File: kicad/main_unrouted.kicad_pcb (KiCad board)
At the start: 2 copper layers, 119.4 x 99.1 mm, 41 parts, among them J1 Barrel_Jack, SW1 Reset, SW6 SW_DIP_x08, U1 KM1810VM88, U10 L7805, U11 15 MHz, U12 8255, U13 74HC273, U14 74HC244, U2 W27C512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

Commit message: Corrected version of v1 PCB
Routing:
- net GND: track 528.8 -> 137.4 mm
- net +5V: track 482.1 -> 115.9 mm
- net AD_{7}: track 231.3 -> 0.00 mm
- net AD_{4}: track 208.0 -> 0.00 mm, vias 2 -> 0
- net AD_{5}: track 196.6 -> 0.00 mm
- net AD_{6}: track 196.3 -> 0.00 mm
- net AD_{3}: track 194.8 -> 0.00 mm, vias 1 -> 0
- net AD_{2}: track 176.7 -> 0.00 mm, vias 2 -> 0
- net ~{RD}: track 175.7 -> 0.00 mm, vias 1 -> 0
- net A_{15}: track 171.3 -> 0.00 mm
- net AD_{0}: track 167.7 -> 0.00 mm, vias 2 -> 0
- net AD_{1}: track 166.1 -> 0.00 mm, vias 2 -> 0
- net A_{0}: track 158.5 -> 0.00 mm, vias 3 -> 0
- net A_{1}: track 152.0 -> 0.00 mm, vias 2 -> 0
- net A_{17}: track 148.6 -> 0.00 mm, vias 2 -> 0
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
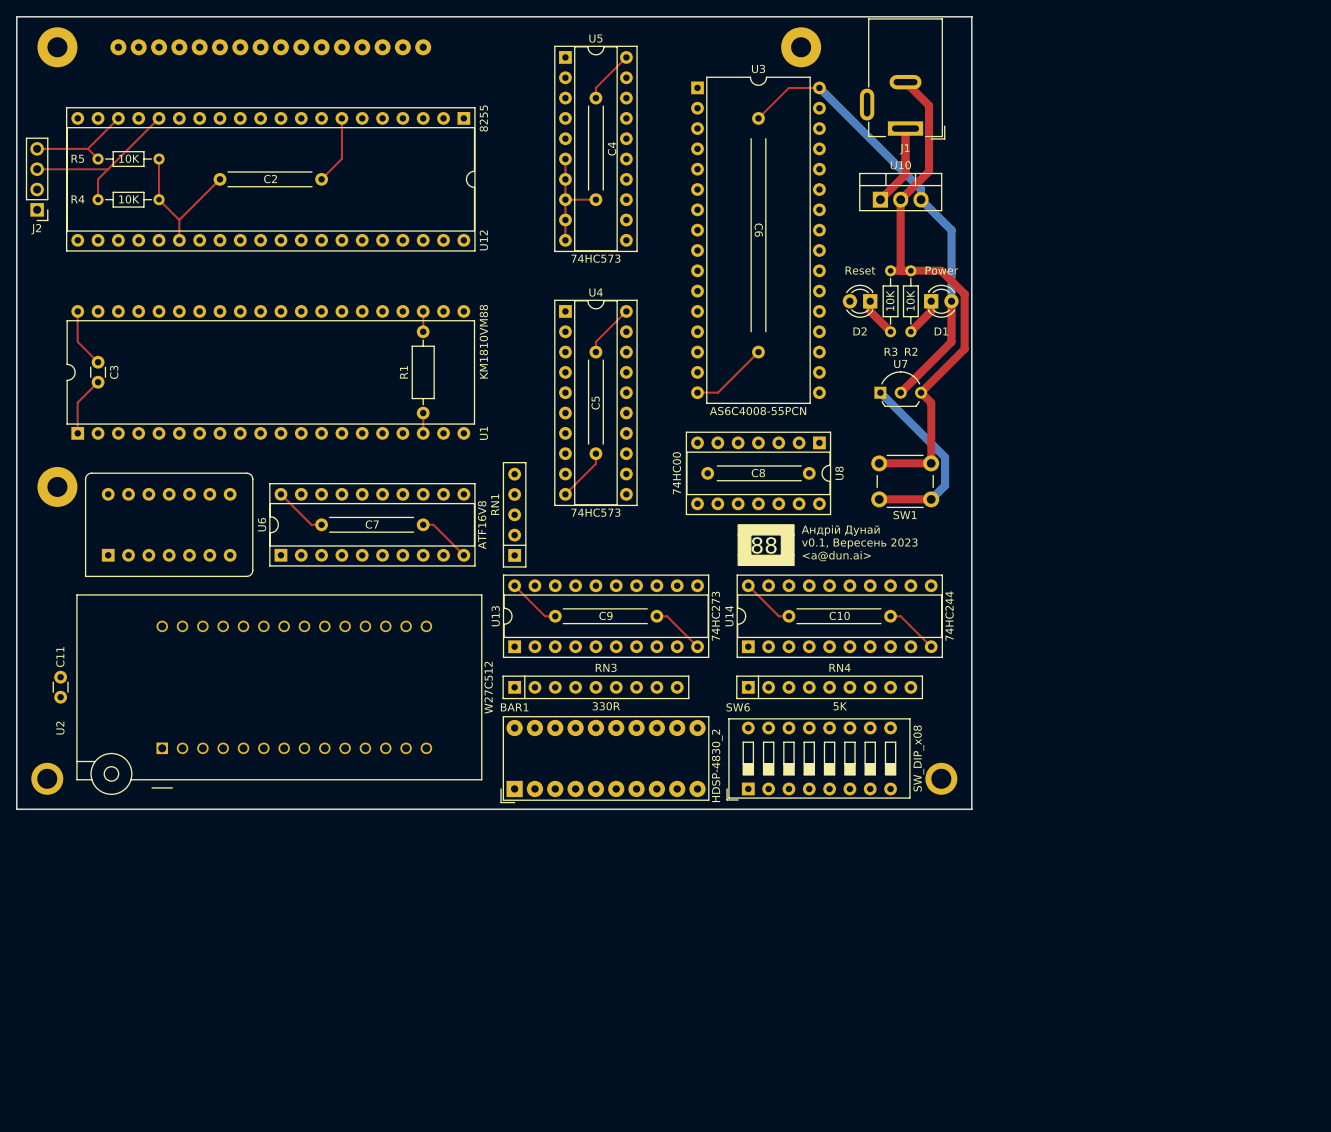
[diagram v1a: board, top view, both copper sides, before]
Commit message: Add I/O sheet
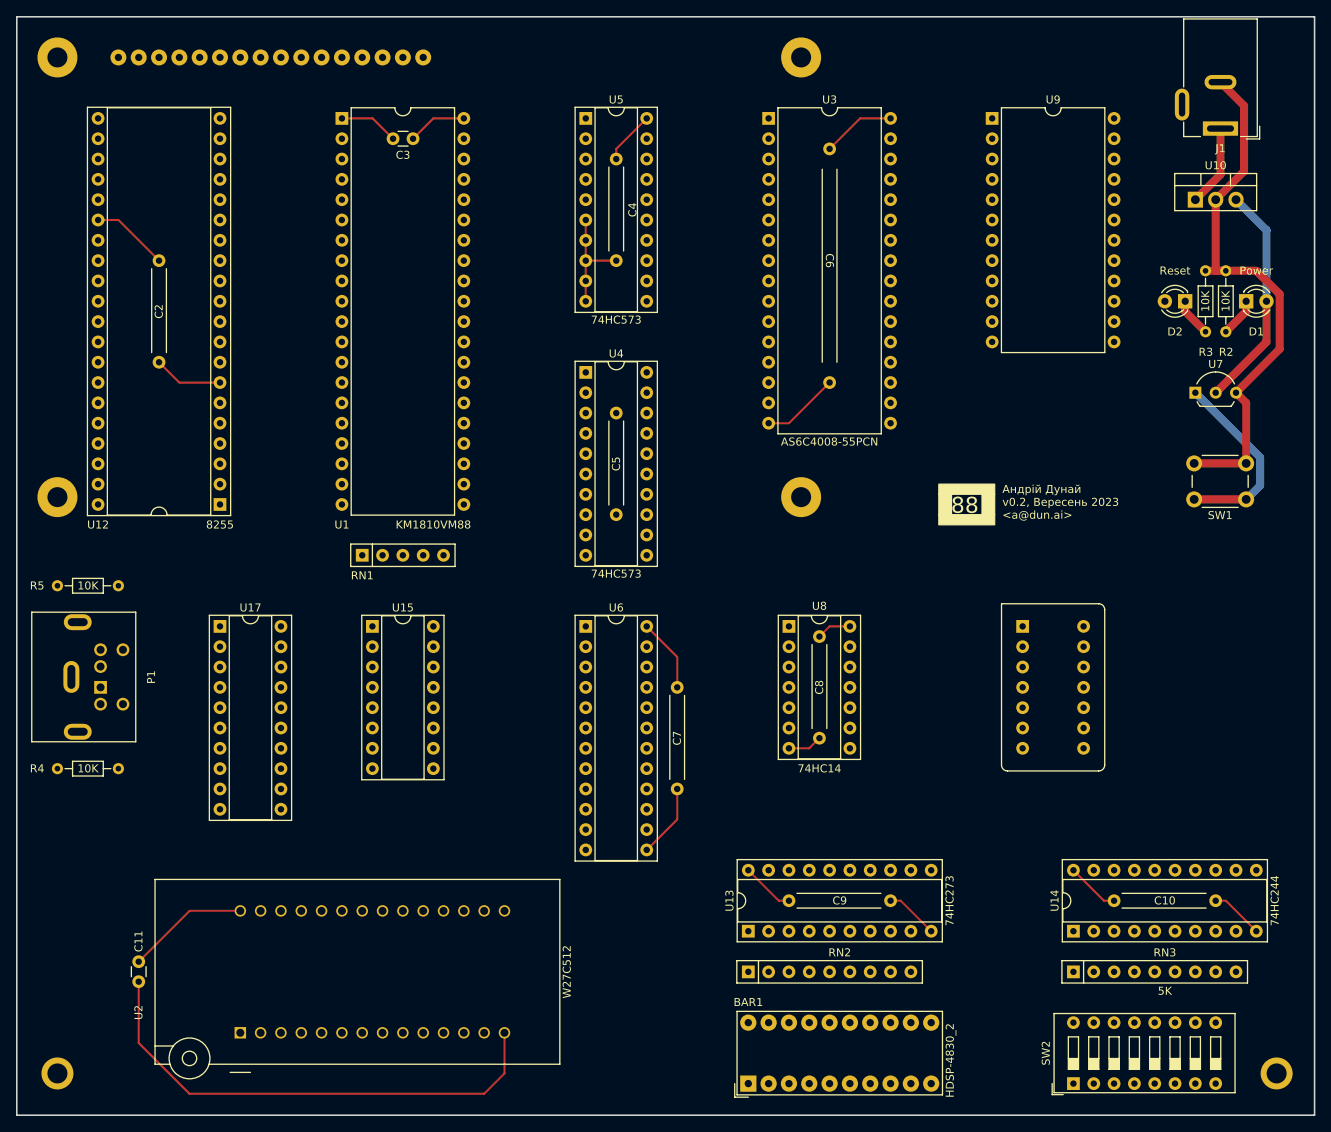
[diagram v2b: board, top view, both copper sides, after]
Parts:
- removed J2: ~, Connector_PinHeader_2.54mm:PinHeader_1x04_P2.54mm_Vertical
- removed R1: 10K, Resistor_THT:R_Axial_DIN0207_L6.3mm_D2.5mm_P10.16mm_Horizontal
- removed RN4: 5K, Resistor_THT:R_Array_SIP9
- removed SW6: SW_DIP_x08, Button_Switch_THT:SW_DIP_SPSTx08_Slide_9.78x22.5mm_W7.62mm_P2.54mm
- added P1: Mini-DIN_6pins_ver3, Custom_Footprints:Connector_Mini-DIN_Female_6Pin_2rows, F.Cu at (25.7, -25.4)
- added RN2: 330R, Resistor_THT:R_Array_SIP9, F.Cu at (106.7, 10.2)
- added SW2: SW_DIP_x08, Button_Switch_THT:SW_DIP_SPSTx08_Slide_9.78x22.5mm_W7.62mm_P2.54mm, F.Cu at (147.3, 24.1)
- added U15: 74HC148, Package_DIP:DIP-16_W7.62mm_Socket, F.Cu at (59.7, -33.0)
- added U17: 74HC244, Package_DIP:DIP-20_W7.62mm_Socket, F.Cu at (40.6, -33.0)
- added U9: 8253, Package_DIP:DIP-24_W15.24mm, F.Cu at (137.2, -96.5)
- RN3: value 330R -> 5K
- U6: value ATF16V8 -> GAL22V10; footprint Package_DIP:DIP-20_W7.62mm_Socket -> Package_DIP:DIP-24_W7.62mm_Socket
- U8: value 74HC00 -> 74HC14
- moved U11 112.1 mm to (144.6, -25.4), turned to -90 degrees
- moved RN3 78.4 mm to (147.3, 10.2)
- moved R4 71.3 mm to (27.9, -15.2)
- moved U12 57.1 mm to (40.6, -48.3), turned to 180 degrees
- moved H2 55.8 mm to (172.7, 22.9)
- moved C10 54.0 mm to (152.4, 1.27)
- moved U14 54.0 mm to (147.3, 5.08)
- moved R5 53.6 mm to (27.9, -38.1)
- moved U1 51.4 mm to (55.9, -96.5), turned to 0 degrees
- moved C7 48.9 mm to (97.8, -25.4), turned to -90 degrees
- moved C3 48.3 mm to (64.8, -94.0), turned to 180 degrees
- moved BAR1 47.0 mm to (106.7, 24.1)
- moved C9 46.0 mm to (111.8, 1.27)
- moved U13 46.0 mm to (106.7, 5.08)
- moved R3 39.4 mm to (163.8, -69.8)
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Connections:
- BAR1 pad 13: Net-(RN3-R8) -> Net-(RN2-R8)
- BAR1 pad 14: Net-(RN3-R7) -> Net-(RN2-R7)
- BAR1 pad 15: Net-(RN3-R6) -> Net-(RN2-R6)
- BAR1 pad 16: Net-(RN3-R5) -> Net-(RN2-R5)
- BAR1 pad 17: Net-(RN3-R4) -> Net-(RN2-R4)
- BAR1 pad 18: Net-(RN3-R3) -> Net-(RN2-R3)
- BAR1 pad 19: Net-(RN3-R2) -> Net-(RN2-R2)
- BAR1 pad 20: Net-(RN3-R1) -> Net-(RN2-R1)
- SW1 pad 1: Net-(U7-~{RST}) -> ~{RES}
- U1 pad 18: INT -> INTR
- U1 pad 24: unconnected-(U1-~{INTA}-Pad24) -> ~{INTA}
- U12 pad 14: INT -> Net-(U12-PC0)
- U13 pad 1: Net-(U13-~{Mr}) -> ~{RES}
- U14 pad 11: Net-(RN4-R8) -> Net-(RN3-R8)
- U14 pad 13: Net-(RN4-R7) -> Net-(RN3-R7)
- U14 pad 15: Net-(RN4-R6) -> Net-(RN3-R6)
- U14 pad 17: Net-(RN4-R5) -> Net-(RN3-R5)
- U14 pad 2: Net-(RN4-R1) -> Net-(RN3-R1)
- U14 pad 4: Net-(RN4-R2) -> Net-(RN3-R2)
- U14 pad 6: Net-(RN4-R3) -> Net-(RN3-R3)
- U14 pad 8: Net-(RN4-R4) -> Net-(RN3-R4)
- U6 pad 10: GND -> unconnected-(U6-I-Pad10)
- U6 pad 11: GND -> unconnected-(U6-I-Pad11)
- U6 pad 12: unconnected-(U6-IO8-Pad12) -> GND
- U6 pad 13: Net-(U6-IO7) -> GND
- U6 pad 15: IO~{EN} -> Net-(U6-I/O/Q-Pad15)
- U6 pad 16: IN~{EN} -> unconnected-(U6-I/O/Q-Pad16)
- U6 pad 17: OUT~{EN} -> Net-(U6-I/O/Q-Pad17)
- U6 pad 18: RAM~{EN} -> TIMER~{EN}
- U6 pad 19: ROM~{EN} -> IO~{EN}
- U6 pad 20: +5V -> IN~{EN}
- U7 pad 1: Net-(U7-~{RST}) -> ~{RES}
- U8 pad 1: Net-(U6-IO7) -> Net-(U6-I/O/Q-Pad15)
- U8 pad 10: Net-(U7-~{RST}) -> ~{INT1}
- U8 pad 11: unconnected-(U8-Pad11) -> Net-(U12-PC0)
- U8 pad 13: unconnected-(U8-Pad13) -> GND
- U8 pad 2: Net-(U6-IO7) -> CLK
- U8 pad 3: CLK -> Net-(U6-I/O/Q-Pad17)
- U8 pad 4: RES -> TIMERCLK
- U8 pad 5: RES -> ~{RES}
- U8 pad 6: Net-(U13-~{Mr}) -> RES
- U8 pad 8: RES -> ~{INT0}
- U8 pad 9: Net-(U7-~{RST}) -> Net-(U9-OUT0)
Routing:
- net GND: track 137.4 -> 197.3 mm
- net ~{RES}: track 0.00 -> 23.9 mm
- net Net-(U7-~{RST}): track 23.9 -> 0.00 mm
- net PS2CLK: track 22.2 -> 0.00 mm
- net PS2DATA: track 13.5 -> 0.00 mm
- net +5V: track 115.9 -> 103.5 mm
- net INT: track 2.54 -> 0.00 mm
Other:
- board size 119.4 x 99.1 mm -> 162.2 x 137.3 mm
- board text added: "Андрій Дунай v0.2, Вересень 2023 <a@dun.ai>"
- board text removed: "Андрій Дунай v0.1, Вересень 2023 <a@dun.ai>"

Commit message: Add UART & uSD card
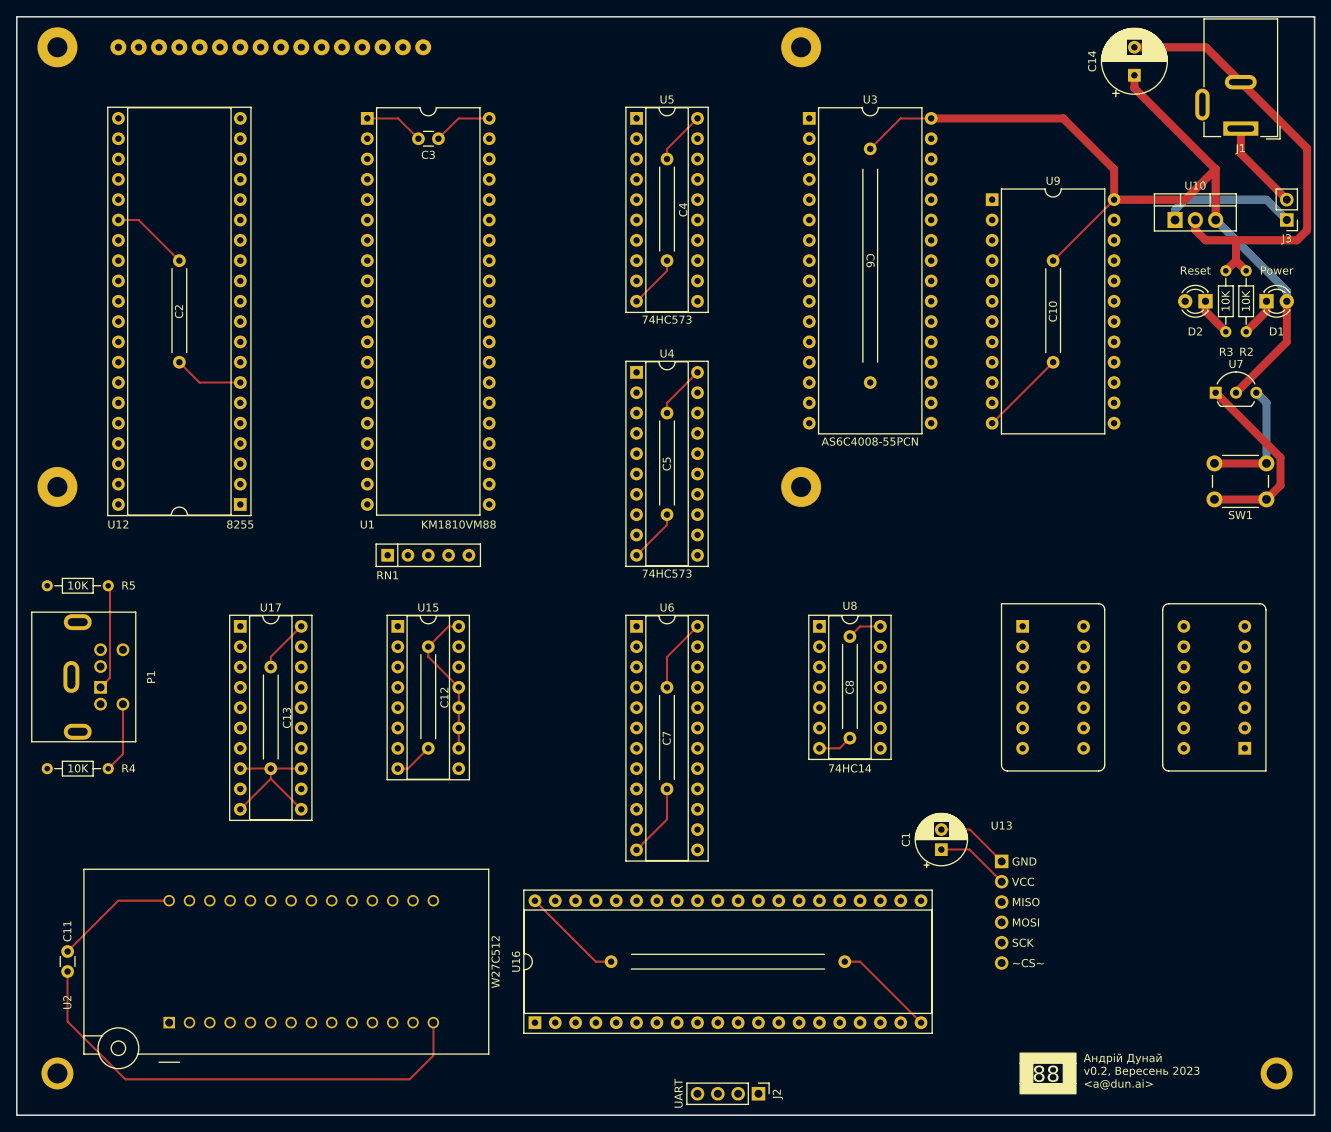
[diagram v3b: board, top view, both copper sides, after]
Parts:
- removed BAR1: HDSP-4830_2, Display:HDSP-4830
- removed RN2: 330R, Resistor_THT:R_Array_SIP9
- removed RN3: 5K, Resistor_THT:R_Array_SIP9
- removed SW2: SW_DIP_x08, Button_Switch_THT:SW_DIP_SPSTx08_Slide_9.78x22.5mm_W7.62mm_P2.54mm
- removed U14: 74HC244, Package_DIP:DIP-20_W7.62mm_Socket
- added C1: 10 uF, Capacitor_THT:CP_Radial_D6.3mm_P2.50mm, F.Cu at (130.8, -5.12)
- added C12: 0.1 uF, footprints:C_Disc_Long, F.Cu at (66.7, -30.5)
- added C13: 0.1 uF, footprints:C_Disc_Long, F.Cu at (47.0, -27.9)
- added C14: 10 uF, Capacitor_THT:CP_Radial_D8.0mm_P3.50mm, F.Cu at (154.9, -101.9)
- added J2: UART, Connector_PinHeader_2.54mm:PinHeader_1x04_P2.54mm_Vertical, F.Cu at (108.0, 25.4)
- added J3: ~, Connector_PinHeader_2.54mm:PinHeader_1x02_P2.54mm_Vertical, F.Cu at (174.0, -83.8)
- added U16: 16550, Package_DIP:DIP-40_W15.24mm_Socket, F.Cu at (80.0, 16.5)
- added U18: 1.8432 MHz, footprints:Oscillator_DIP-8-14, F.Cu at (165.1, -25.4)
- C9: footprint footprints:C_Disc_Long -> footprints:C_Disc_VeryLong
- U13: value 74HC273 -> uSD adapter; footprint Package_DIP:DIP-20_W7.62mm_Socket -> footprints:MicroSD-Adapter
- moved C10 80.4 mm to (144.8, -78.7), turned to -90 degrees
- moved U13 32.5 mm to (135.8, -9.36), turned to 0 degrees
- moved C9 17.6 mm to (95.9, 8.89)
- moved U9 10.2 mm to (137.2, -86.4)
- moved C11 8.98 mm to (21.6, 7.62)
- moved U2 8.98 mm to (34.3, 16.5)
- moved R4 8.89 mm to (19.1, -15.2), turned to 0 degrees
- moved R5 8.89 mm to (19.1, -38.1), turned to 0 degrees
- moved C4 6.35 mm to (96.5, -91.4)
- moved C5 6.35 mm to (96.5, -59.7)
- moved U4 6.35 mm to (92.7, -64.8)
- moved U5 6.35 mm to (92.7, -96.5)
- moved U6 6.35 mm to (92.7, -33.0)
- moved C6 5.08 mm to (121.9, -86.4)
- moved U3 5.08 mm to (114.3, -96.5)
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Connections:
- net Net-(U11-OUT) renamed MCLK
- J1 pad 1: Net-(U10-IN) -> Net-(J3-Pin_2)
- U1 pad 31: unconnected-(U1-HOLD-Pad31) -> GND
- U10 pad 1: Net-(U10-IN) -> Net-(J3-Pin_1)
- U13 pad 1: ~{RES} -> GND
- U13 pad 2: Net-(U13-Q0) -> +5V
- U13 pad 3: AD_{0} -> Net-(U13-MISO)
- U13 pad 4: AD_{1} -> Net-(U13-MOSI)
- U15 pad 2: +5V -> ~{INT2}
- U6 pad 10: unconnected-(U6-I-Pad10) -> IO/~{M}
- U6 pad 16: unconnected-(U6-I/O/Q-Pad16) -> Net-(U6-I/O/Q-Pad16)
- U6 pad 17: Net-(U6-I/O/Q-Pad17) -> unconnected-(U6-I/O/Q-Pad17)
- U6 pad 18: TIMER~{EN} -> unconnected-(U6-I/O/Q-Pad18)
- U6 pad 19: IO~{EN} -> UART~{EN}
- U6 pad 20: IN~{EN} -> TIMER~{EN}
- U6 pad 21: OUT~{EN} -> IO~{EN}
- U6 pad 3: A_{16} -> A_{9}
- U6 pad 4: A_{17} -> A_{16}
- U6 pad 5: A_{18} -> A_{17}
- U6 pad 6: A_{19} -> A_{18}
- U6 pad 7: ~{RD} -> A_{19}
- U6 pad 8: ~{WR} -> ~{RD}
- U6 pad 9: IO/~{M} -> ~{WR}
- U8 pad 12: unconnected-(U8-Pad12) -> ~{INT2}
- U8 pad 13: GND -> Net-(U16-INTR)
- U8 pad 3: Net-(U6-I/O/Q-Pad17) -> Net-(U6-I/O/Q-Pad16)
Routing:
- net +5V: track 103.5 -> 220.7 mm
- net GND: track 197.3 -> 235.8 mm
- net Net-(J3-Pin_1): track 0.00 -> 16.8 mm
- net PS2DATA: track 0.00 -> 13.3 mm
- net Net-(J3-Pin_2): track 0.00 -> 11.3 mm
- net Net-(U10-IN): track 10.2 -> 0.00 mm
- net PS2CLK: track 0.00 -> 8.82 mm

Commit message: Move chips to center/bottom
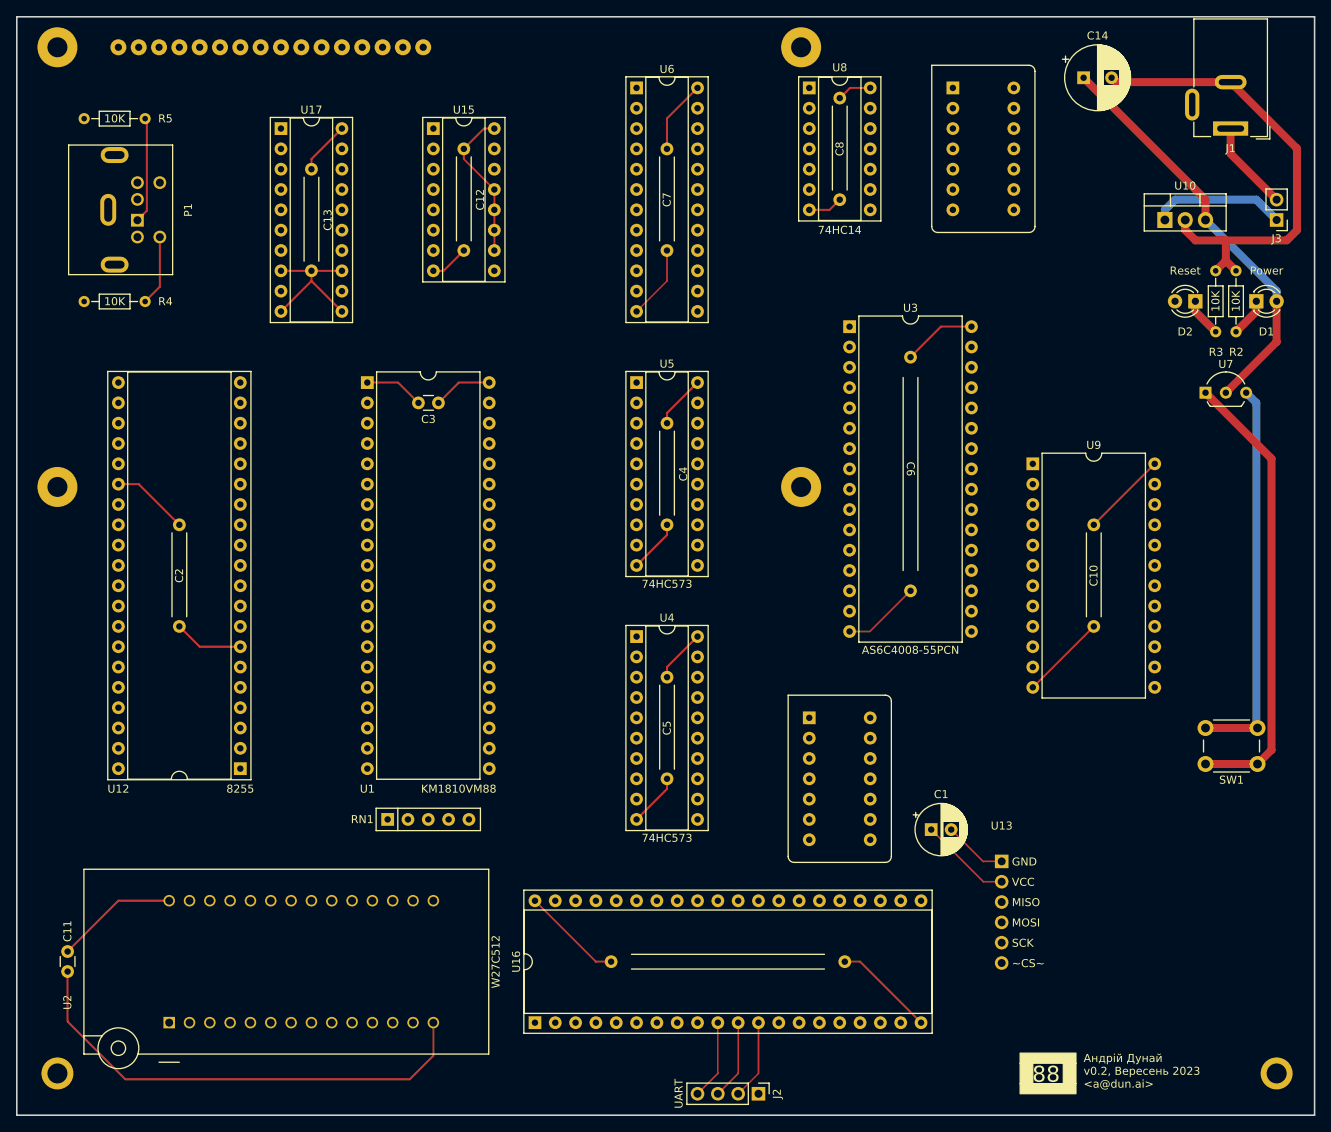
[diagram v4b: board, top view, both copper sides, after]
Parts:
- moved U11 67.9 mm to (135.9, -92.7)
- moved C8 67.3 mm to (118.1, -99.1)
- moved U8 67.3 mm to (114.3, -100.3)
- moved C7 67.3 mm to (96.5, -92.7)
- moved U6 67.3 mm to (92.7, -100.3)
- moved C13 62.4 mm to (52.1, -90.2)
- moved U17 62.4 mm to (48.3, -95.2)
- moved U15 62.4 mm to (67.3, -95.2)
- moved C12 62.4 mm to (71.1, -92.7)
- moved P1 58.6 mm to (30.3, -83.8)
- moved R4 58.6 mm to (23.7, -73.6)
- moved R5 58.6 mm to (23.7, -96.5)
- moved U18 48.5 mm to (117.9, -14.0), turned to -90 degrees
- moved C10 33.4 mm to (149.9, -45.7)
- moved U9 33.4 mm to (142.2, -53.3)
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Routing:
- net GND: track 235.8 -> 277.4 mm
- net ~{RES}: track 23.9 -> 57.1 mm
- net +5V: track 220.7 -> 191.2 mm
- net Net-(J2-Pin_4): track 0.00 -> 9.94 mm
- net Net-(J2-Pin_3): track 0.00 -> 9.94 mm
